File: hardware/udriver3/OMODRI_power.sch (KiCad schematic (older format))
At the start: 82 parts, among them U2 MAX17502FxTB, U3 TMS320F28388D, U4 MPM3804GG, U5 MPM3804GG, U6 REF6230, U7 OPA388

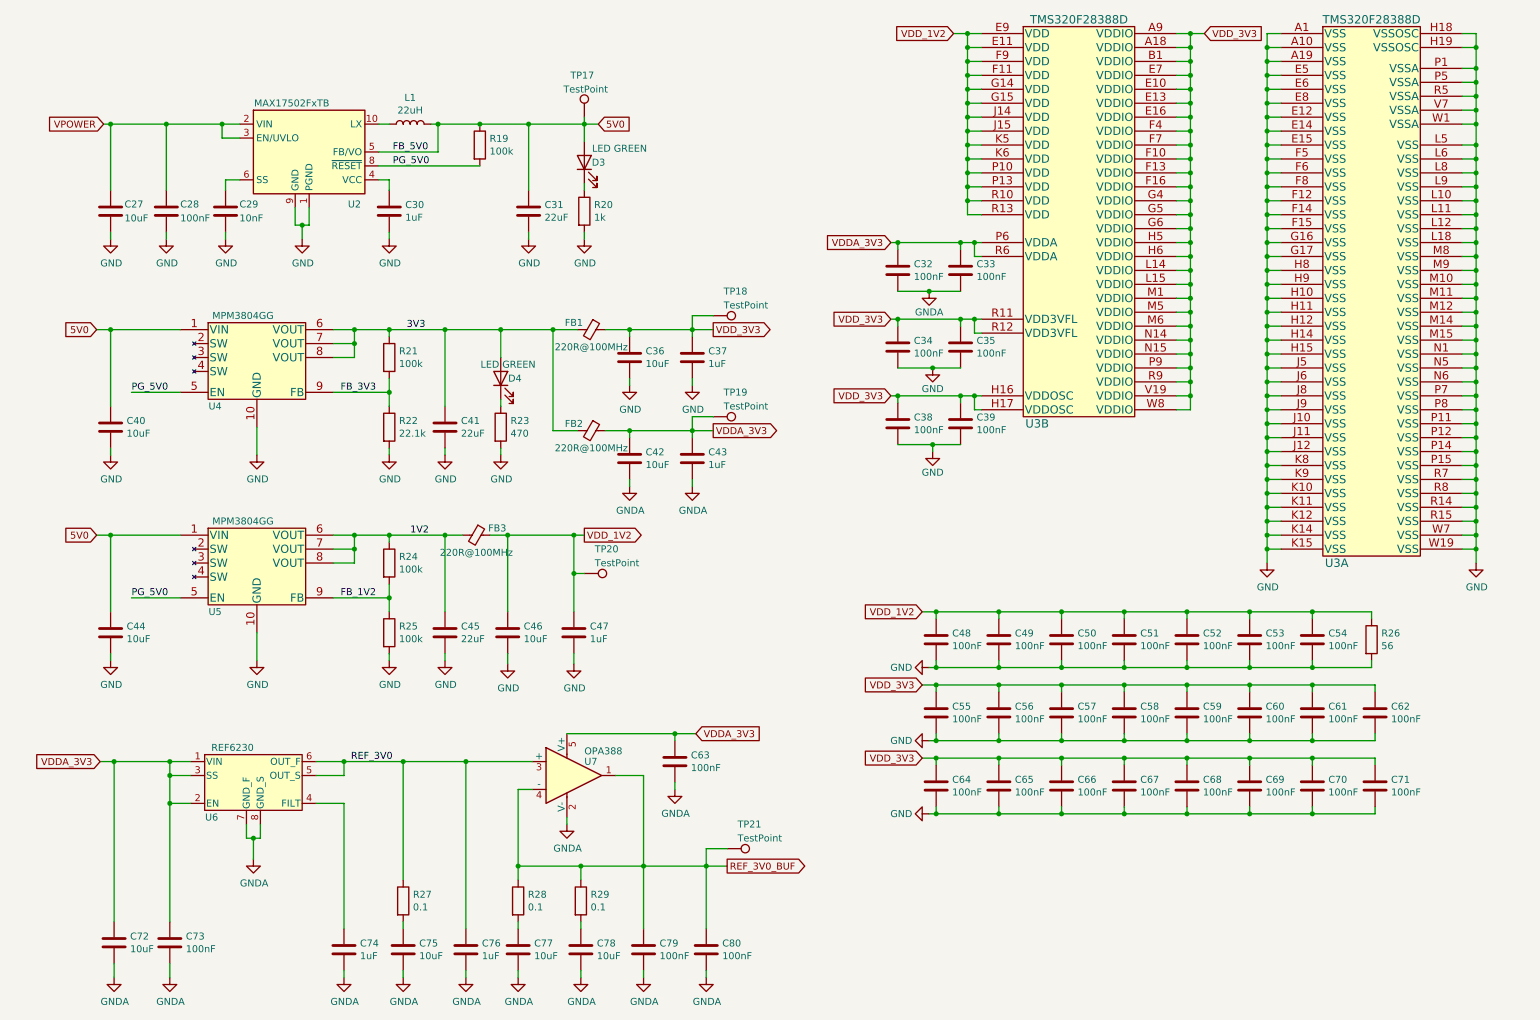
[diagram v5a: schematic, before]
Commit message: Update of the schematics. Driver and power files split. Placement starting.
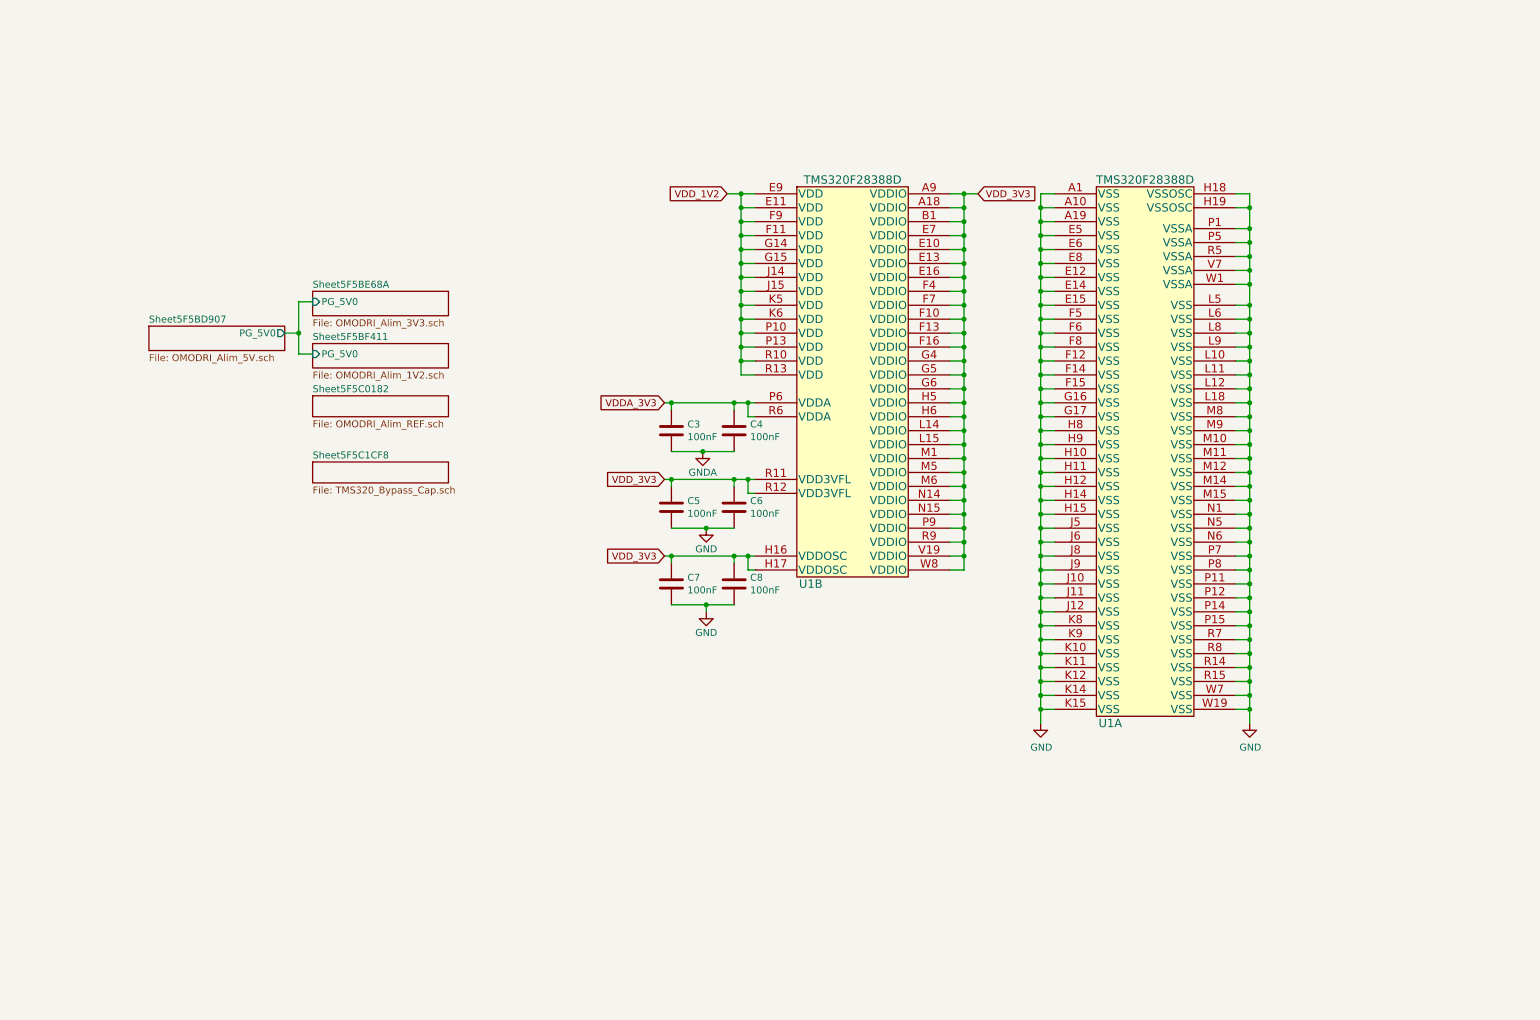
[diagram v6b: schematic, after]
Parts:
- removed C27: 10uF, Capacitor_SMD:C_1210_3225Metric, symbol Device:C
- removed C28: 100nF, Capacitor_SMD:C_0805_2012Metric, symbol Device:C
- removed C29: 10nF, Capacitor_SMD:C_0201_0603Metric, symbol Device:C
- removed C30, C37, C43, C47, C74, C76: 1uF, Capacitor_SMD:C_0201_0603Metric, symbol Device:C
- removed C31, C41, C45: 22uF, Capacitor_SMD:C_0603_1608Metric, symbol Device:C
- removed C36, C40, C42, C44, C46, C72, C75, C77, C78: 10uF, Capacitor_SMD:C_0603_1608Metric, symbol Device:C
- removed C48, C49, C50, C51, C52, C53, C54, C55, C56, C57, C58, C59, C60, C61, C62, C63, C64, C65, C66, C67, C68, C69, C70, C71, C73, C79, C80: 100nF, Capacitor_SMD:C_0201_0603Metric, symbol Device:C
- removed D3, D4: LED GREEN, LED_SMD:LED_0402_1005Metric, symbol Device:LED
- removed FB1, FB2, FB3: 220R@100MHz, Inductor_SMD:L_0603_1608Metric, symbol Device:Ferrite_Bead_Small
- removed L1: 22uH, udrive3:L_coilcraft_LPS62xx, symbol Device:L
- removed R19, R21, R24, R25: 100k, Resistor_SMD:R_0201_0603Metric, symbol Device:R
- removed R20: 1k, Resistor_SMD:R_0201_0603Metric, symbol Device:R
- removed R22: 22.1k, Resistor_SMD:R_0201_0603Metric, symbol Device:R
- removed R23: 470, Resistor_SMD:R_0201_0603Metric, symbol Device:R
- removed R26: 56, Resistor_SMD:R_0201_0603Metric, symbol Device:R
- removed R27, R28, R29: 0.1, Resistor_SMD:R_0201_0603Metric, symbol Device:R
- removed TP17, TP18, TP19, TP20, TP21: TestPoint, TestPoint:TestPoint_Pad_D1.0mm, symbol Connector:TestPoint
- removed U2: MAX17502FxTB, Package_DFN_QFN:TDFN-10-1EP_2x3mm_P0.5mm_EP0.9x2mm, symbol Regulator_Switching:MAX17501FxTB
- removed U4, U5: MPM3804GG, udrive3:QFN-10_2x2mm_P0.5mm, symbol omodri_lib:MPM3804GG
- removed U6: REF6230, Package_SO:VSSOP-8_3.0x3.0mm_P0.65mm, symbol omodri_lib:REF6230
- removed U7: OPA388, Package_TO_SOT_SMD:TSOT-23-5, symbol omodri_lib:OPA388
- U1: renamed from U3; footprint udrive3:NFBGA_337 -> udriver3:NFBGA_337
- renumbered C32 to C3, C33 to C4, C34 to C5, C35 to C6, C38 to C7, C39 to C8
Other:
- moved on the sheet: C3, C4, C5, C6, C7, C8, U1A, U1B

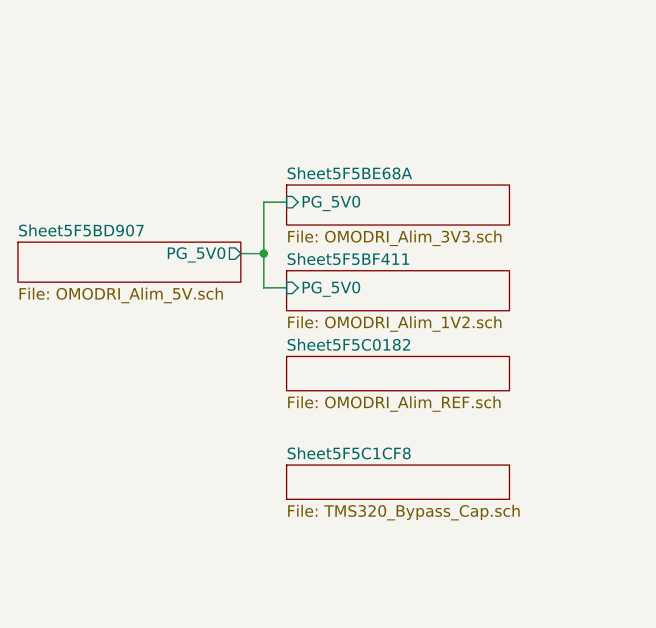
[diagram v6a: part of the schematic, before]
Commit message: Update of the schematics. Switches on GPIO72 & GPIO84 are missing. J1, J2 & J14 must be merged and connector placement optimized. TCXO must be changed from 20MHz to 25MHz for EtherCAT compatibility. PCB is partially routed in 6-Layers (mainly power supplies and and transistors). 8-Layers will be necessary.
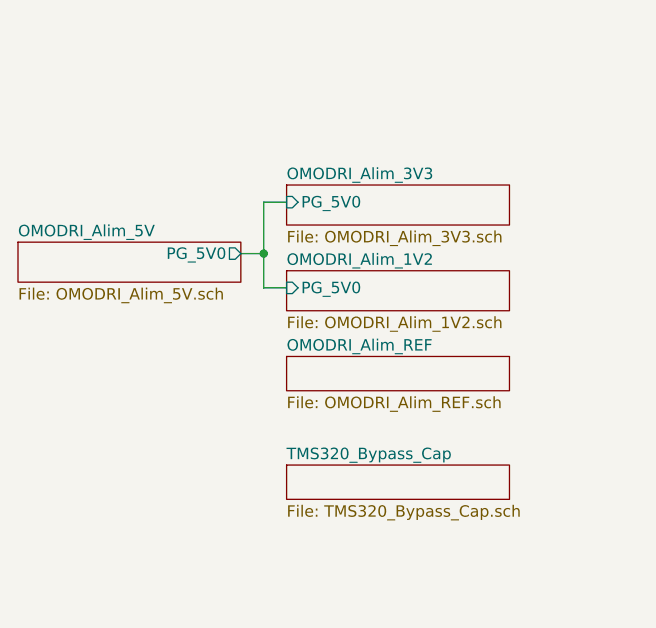
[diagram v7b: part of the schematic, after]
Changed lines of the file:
@@
 S 1375 2800 975  175
 U 5F5BD908
-F0 "Sheet5F5BD907" 50
+F0 "OMODRI_Alim_5V" 50
 F1 "OMODRI_Alim_5V.sch" 50
 F2 "PG_5V0" O R 2350 2850 50
@@
 S 2550 2550 975  175
 U 5F5BE68B
-F0 "Sheet5F5BE68A" 50
+F0 "OMODRI_Alim_3V3" 50
 F1 "OMODRI_Alim_3V3.sch" 50
 F2 "PG_5V0" I L 2550 2625 50
@@
 S 2550 2925 975  175
 U 5F5BF412
-F0 "Sheet5F5BF411" 50
+F0 "OMODRI_Alim_1V2" 50
 F1 "OMODRI_Alim_1V2.sch" 50
 F2 "PG_5V0" I L 2550 3000 50
@@
 S 2550 3300 975  150
 U 5F5C0183
-F0 "Sheet5F5C0182" 50
+F0 "OMODRI_Alim_REF" 50
 F1 "OMODRI_Alim_REF.sch" 50
 $EndSheet
@@
 S 2550 3775 975  150
 U 5F5C1CF9
-F0 "Sheet5F5C1CF8" 50
+F0 "TMS320_Bypass_Cap" 50
 F1 "TMS320_Bypass_Cap.sch" 50
 $EndSheet
